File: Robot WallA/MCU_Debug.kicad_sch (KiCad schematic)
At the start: 10 parts, among them J11 USB_B_Micro, U5 FT230XS

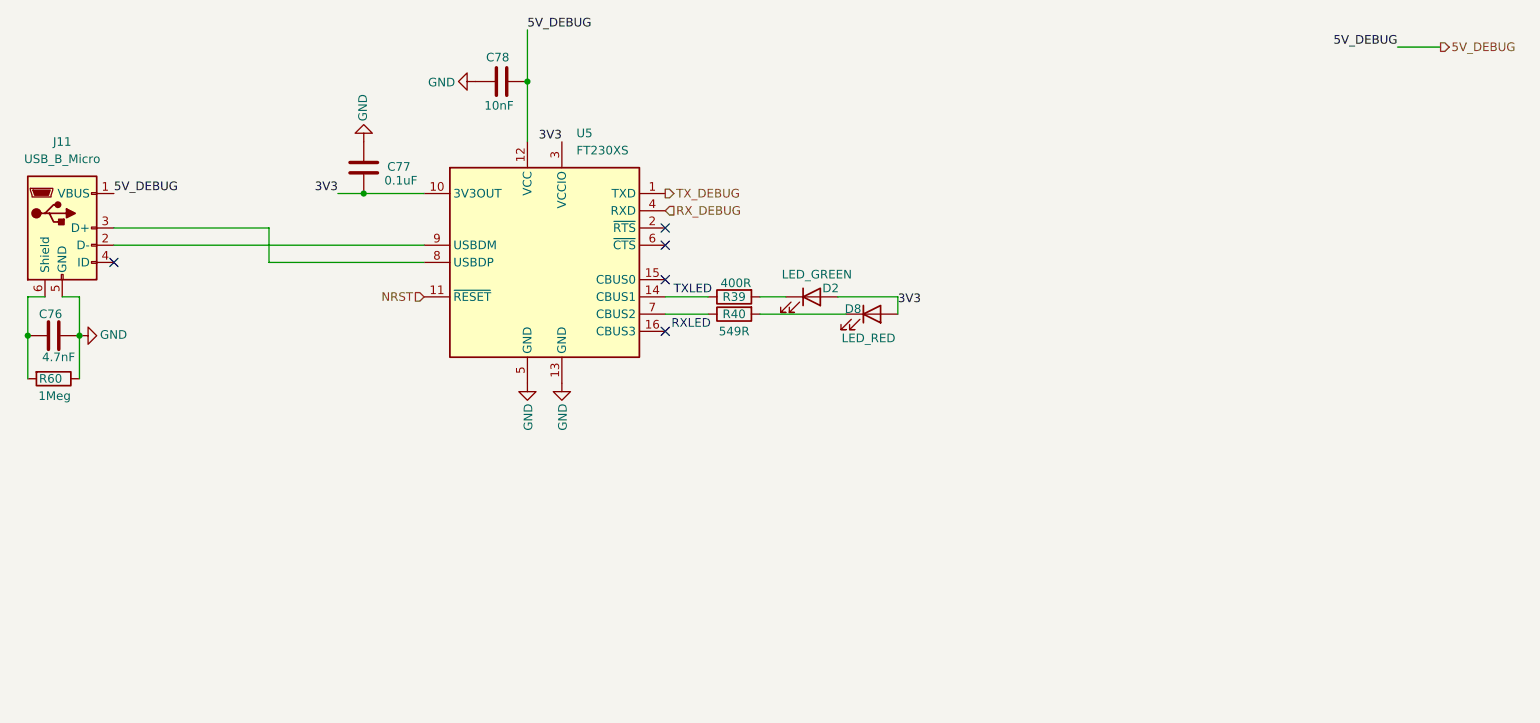
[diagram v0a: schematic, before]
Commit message: Continued to link MCU pins, Added a sheet for servomotors and optional 2 DC motors.
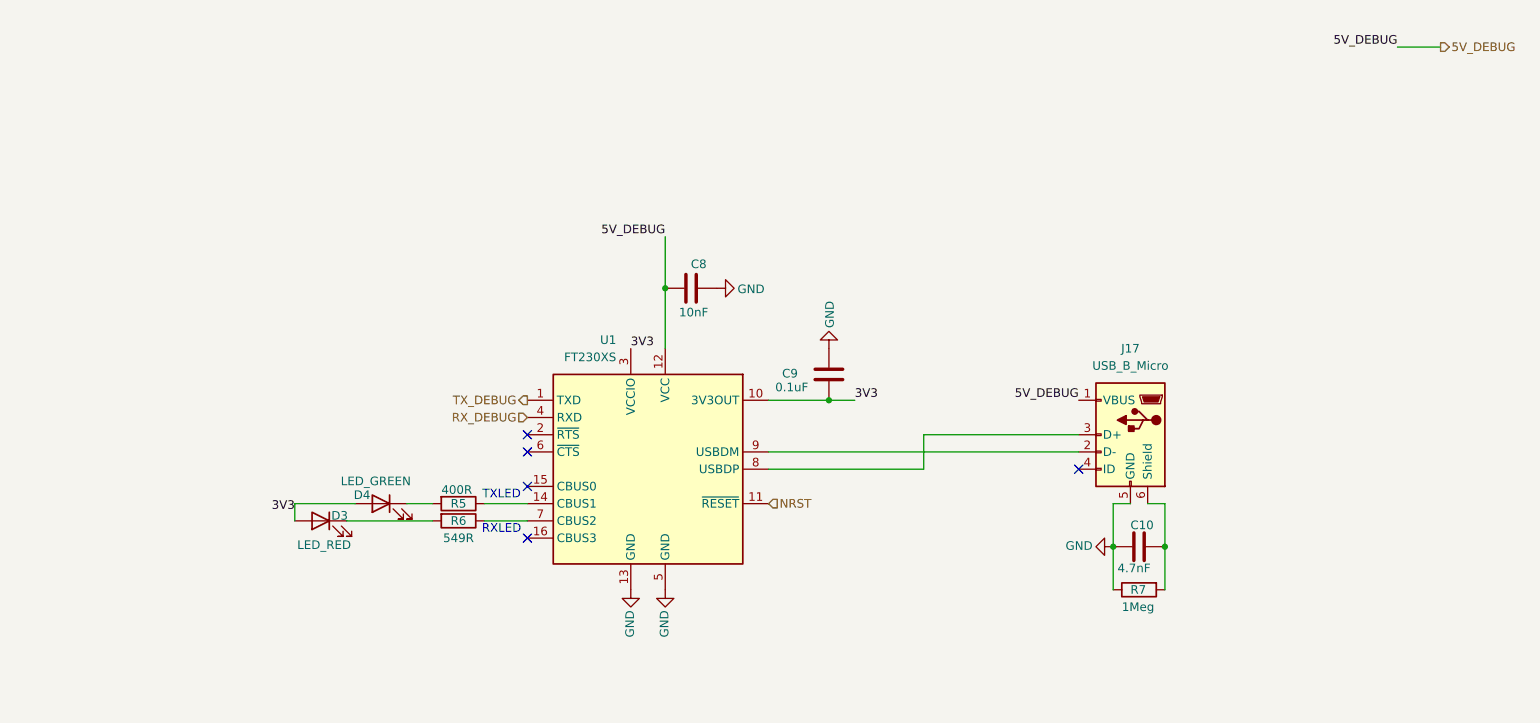
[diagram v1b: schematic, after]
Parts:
- renumbered C76 to C10, C78 to C8, C77 to C9, D8 to D3, D2 to D4, J11 to J17, R39 to R5, R40 to R6, R60 to R7, U5 to U1
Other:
- moved on the sheet: C10, C8, C9, D3, D4, J17, R5, R6, R7, U1

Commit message: Defined every footprints
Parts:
- C34: renamed from C9; value 0.1uF -> 100nF
- R27: renamed from R5; footprint Resistor_SMD:R_0603_1608Metric -> Resistor_SMD:R_0603_1608Metric_Pad0.98x0.95mm_HandSolder
- R28: renamed from R6; footprint Resistor_SMD:R_0603_1608Metric -> Resistor_SMD:R_0603_1608Metric_Pad0.98x0.95mm_HandSolder; Manufacturer_Part_Number RC0603FR-07549RL -> (none)
- renumbered C8 to C33, C10 to C35, D4 to D1, D3 to D2, J17 to J4, R7 to R29
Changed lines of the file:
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@@
 		(on_board yes)
 		(dnp no)
-		(property "Reference" "#PWR023"
+		(property "Reference" "#PWR038"
 			(at 130.81 106.68 0)
 			(effects
@@
 			(project "PCB"
 				(path "/117fd49e-499d-4b54-b58c-f6b538ecca4a/b9176f6a-4299-4bca-a59b-5ff3df09c616/17777bae-0c68-45a7-8f55-4db398213b8b"
-					(reference "#PWR023")
+					(reference "#PWR038")
 					(unit 1)
 				)
@@
 		(on_board yes)
 		(dnp no)
-		(property "Reference" "D3"
+		(property "Reference" "D2"
 			(at 87.884 89.408 0)
 			(effects
@@
 			)
 		)
-		(property "Sim.Pins" "1=K 2=A"
-			(at 85.09 90.17 0)
-			(effects
-				(font
-					(size 1.27 1.27)
-				)
-				(hide yes)
-			)
-		)
 		(pin "2"
 		)
@@
 			(project "PCB"
 				(path "/117fd49e-499d-4b54-b58c-f6b538ecca4a/b9176f6a-4299-4bca-a59b-5ff3df09c616/17777bae-0c68-45a7-8f55-4db398213b8b"
-					(reference "D3")
+					(reference "D2")
 					(unit 1)
 				)
@@
 		(on_board yes)
 		(dnp no)
-		(property "Reference" "#PWR027"
+		(property "Reference" "#PWR037"
 			(at 195.58 93.98 0)
 			(effects
@@
 			(project "PCB"
 				(path "/117fd49e-499d-4b54-b58c-f6b538ecca4a/b9176f6a-4299-4bca-a59b-5ff3df09c616/17777bae-0c68-45a7-8f55-4db398213b8b"
-					(reference "#PWR027")
+					(reference "#PWR037")
 					(unit 1)
 				)
@@
 		(on_board yes)
 		(dnp no)
-		(property "Reference" "R7"
+		(property "Reference" "R29"
 			(at 204.47 100.33 90)
 			(effects
@@
 			(project "PCB"
 				(path "/117fd49e-499d-4b54-b58c-f6b538ecca4a/b9176f6a-4299-4bca-a59b-5ff3df09c616/17777bae-0c68-45a7-8f55-4db398213b8b"
-					(reference "R7")
+					(reference "R29")
 					(unit 1)
 				)
@@
 		(on_board yes)
 		(dnp no)
-		(property "Reference" "C10"
+		(property "Reference" "C35"
 			(at 204.47 90.805 90)
 			(effects
@@
 			(project "PCB"
 				(path "/117fd49e-499d-4b54-b58c-f6b538ecca4a/b9176f6a-4299-4bca-a59b-5ff3df09c616/17777bae-0c68-45a7-8f55-4db398213b8b"
-					(reference "C10")
+					(reference "C35")
 					(unit 1)
 				)
@@
 		(on_board yes)
 		(dnp no)
-		(property "Reference" "#PWR026"
+		(property "Reference" "#PWR036"
 			(at 160.02 58.42 0)
 			(effects
@@
 			(project "PCB"
 				(path "/117fd49e-499d-4b54-b58c-f6b538ecca4a/b9176f6a-4299-4bca-a59b-5ff3df09c616/17777bae-0c68-45a7-8f55-4db398213b8b"
-					(reference "#PWR026")
+					(reference "#PWR036")
 					(unit 1)
 				)
@@
 		(on_board yes)
 		(dnp no)
-		(property "Reference" "#PWR025"
+		(property "Reference" "#PWR035"
 			(at 149.86 55.88 0)
 			(effects
@@
 			(project "PCB"
 				(path "/117fd49e-499d-4b54-b58c-f6b538ecca4a/b9176f6a-4299-4bca-a59b-5ff3df09c616/17777bae-0c68-45a7-8f55-4db398213b8b"
-					(reference "#PWR025")
+					(reference "#PWR035")
 					(unit 1)
 				)
@@
 		(on_board yes)
 		(dnp no)
-		(property "Reference" "D4"
+		(property "Reference" "D1"
 			(at 91.186 86.36 0)
 			(effects
@@
 			(project "PCB"
 				(path "/117fd49e-499d-4b54-b58c-f6b538ecca4a/b9176f6a-4299-4bca-a59b-5ff3df09c616/17777bae-0c68-45a7-8f55-4db398213b8b"
-					(reference "D4")
+					(reference "D1")
 					(unit 1)
 				)
@@
 		(dnp no)
 		(fields_autoplaced yes)
-		(property "Reference" "J17"
+		(property "Reference" "J4"
 			(at 204.47 64.77 0)
 			(effects
@@
 			(project ""
 				(path "/117fd49e-499d-4b54-b58c-f6b538ecca4a/b9176f6a-4299-4bca-a59b-5ff3df09c616/17777bae-0c68-45a7-8f55-4db398213b8b"
-					(reference "J17")
+					(reference "J4")
 					(unit 1)
 				)
@@
 		(on_board yes)
 		(dnp no)
-		(property "Reference" "R6"
+		(property "Reference" "R28"
 			(at 105.41 90.17 90)
 			(effects
@@
 			)
 		)
-		(property "Footprint" "Resistor_SMD:R_0603_1608Metric"
+		(property "Footprint" "Resistor_SMD:R_0603_1608Metric_Pad0.98x0.95mm_HandSolder"
 			(at 105.41 88.392 90)
 			(effects
@@
 			)
 		)
-		(property "Manufacturer_Part_Number" "RC0603FR-07549RL "
+		(property "Manufacturer_Part_Number" ""
 			(at 105.41 90.17 0)
 			(effects
@@
 			(project "PCB"
 				(path "/117fd49e-499d-4b54-b58c-f6b538ecca4a/b9176f6a-4299-4bca-a59b-5ff3df09c616/17777bae-0c68-45a7-8f55-4db398213b8b"
-					(reference "R6")
+					(reference "R28")
 					(unit 1)
 				)
@@
 		(on_board yes)
 		(dnp no)
-		(property "Reference" "C9"
+		(property "Reference" "C34"
 			(at 153.1198 68.4452 0)
 			(effects
@@
 			)
 		)
-		(property "Value" "0.1uF"
+		(property "Value" "100nF"
 			(at 152.1038 70.4772 0)
 			(effects
@@
 			(project "PCB"
 				(path "/117fd49e-499d-4b54-b58c-f6b538ecca4a/b9176f6a-4299-4bca-a59b-5ff3df09c616/17777bae-0c68-45a7-8f55-4db398213b8b"
-					(reference "C9")
+					(reference "C34")
 					(unit 1)
 				)
@@
 		(on_board yes)
 		(dnp no)
-		(property "Reference" "R5"
+		(property "Reference" "R27"
 			(at 105.41 87.63 90)
 			(effects
@@
 			)
 		)
-		(property "Footprint" "Resistor_SMD:R_0603_1608Metric"
+		(property "Footprint" "Resistor_SMD:R_0603_1608Metric_Pad0.98x0.95mm_HandSolder"
 			(at 105.41 85.852 90)
 			(effects
@@
 			(project "PCB"
 				(path "/117fd49e-499d-4b54-b58c-f6b538ecca4a/b9176f6a-4299-4bca-a59b-5ff3df09c616/17777bae-0c68-45a7-8f55-4db398213b8b"
-					(reference "R5")
+					(reference "R27")
 					(unit 1)
 				)
@@
 		(on_board yes)
 		(dnp no)
-		(property "Reference" "#PWR024"
+		(property "Reference" "#PWR039"
 			(at 135.89 106.68 0)
 			(effects
@@
 			(project "PCB"
 				(path "/117fd49e-499d-4b54-b58c-f6b538ecca4a/b9176f6a-4299-4bca-a59b-5ff3df09c616/17777bae-0c68-45a7-8f55-4db398213b8b"
-					(reference "#PWR024")
+					(reference "#PWR039")
 					(unit 1)
 				)
@@
 		(on_board yes)
 		(dnp no)
-		(property "Reference" "C8"
+		(property "Reference" "C33"
 			(at 141.986 52.324 90)
 			(effects
@@
 			(project "PCB"
 				(path "/117fd49e-499d-4b54-b58c-f6b538ecca4a/b9176f6a-4299-4bca-a59b-5ff3df09c616/17777bae-0c68-45a7-8f55-4db398213b8b"
-					(reference "C8")
-					(unit 1)
-				)
+					(reference "C33")
+					(unit 1)
+				)

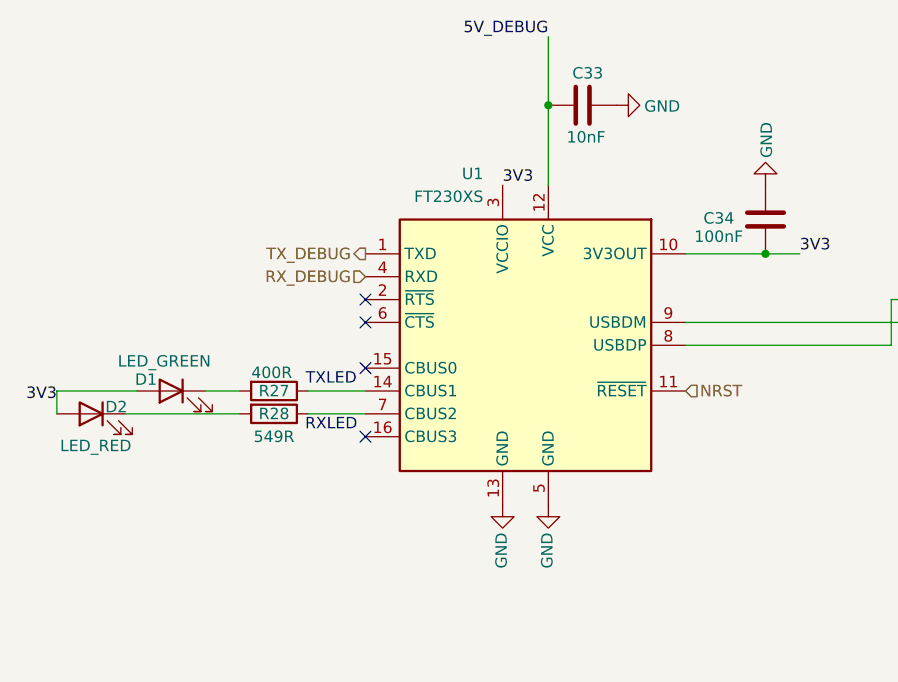
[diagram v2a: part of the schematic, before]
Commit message: Updated USB UART converter, Linked telemeter sensors.
Updated components indicators
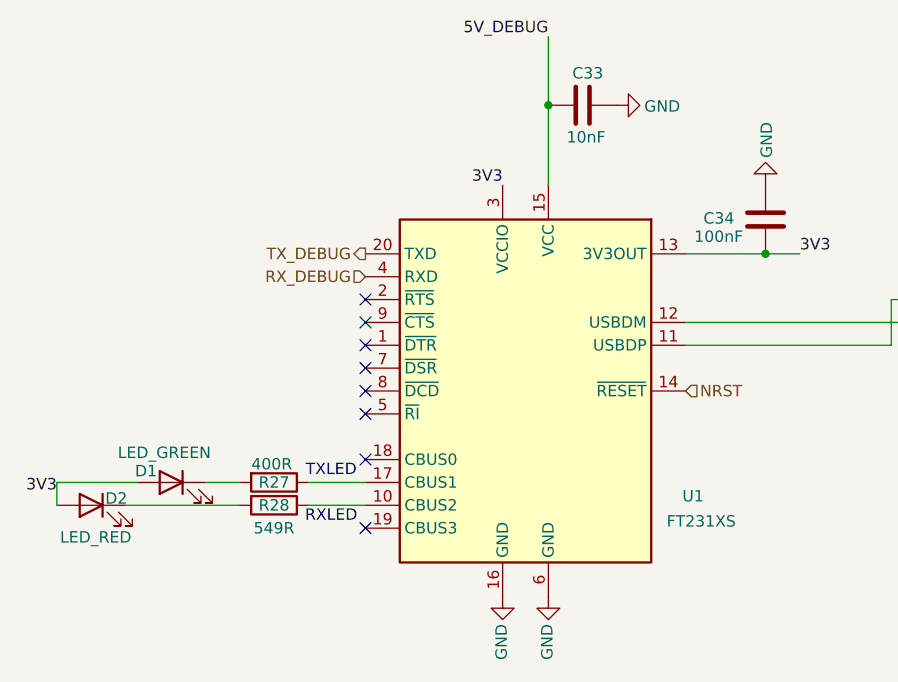
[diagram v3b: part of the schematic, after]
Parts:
- removed U1: FT230XS, Package_SO:SSOP-16_3.9x4.9mm_P0.635mm, symbol Interface_USB:FT230XS
- added U1: FT231XS, Package_SO:SSOP-20_3.9x8.7mm_P0.635mm, symbol Interface_USB:FT231XS
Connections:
- net 3V3: now also U1.13 (3V3OUT), U1.3 (VCCIO)
- net 5V_DEBUG: now also U1.15 (VCC)
- net GND: now also U1.16 (GND), U1.6 (GND)
- net NRST: now also U1.14 (~{RESET})
- net RX_DEBUG: now also U1.4 (RXD)
- net TX_DEBUG: now also U1.20 (TXD)
- net at J4.2 (D-): now also U1.12 (USBDM)
- net at J4.3 (D+): now also U1.11 (USBDP)
- net at R28.1: now also U1.10 (CBUS2)
- net at R27.1: now also U1.17 (CBUS1)
- no-connect marks 5 -> 9

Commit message: Continue to route
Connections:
- net D-: now reaches J4.2 (D-), U1.12 (USBDM)
- net D+: now reaches J4.3 (D+), U1.11 (USBDP)
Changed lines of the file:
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@@
+		)
+	)
+	(label "D-"
+		(at 158.75 80.01 0)
+		(effects
+			(font
+				(size 1.27 1.27)
+				(thickness 0.254)
+				(bold yes)
+			)
+			(justify left bottom)
+		)
+	)
+	(label "D+"
+		(at 158.75 82.55 0)
+		(effects
+			(font
+				(size 1.27 1.27)
+				(thickness 0.254)
+				(bold yes)
+			)
+			(justify left bottom)
+		)
+	)
+	(label "D+"
+		(at 196.85 114.3 180)
+		(effects
+			(font
+				(size 1.27 1.27)
+				(thickness 0.254)
+				(bold yes)
+			)
+			(justify right bottom)
+		)
+	)
+	(label "D-"
+		(at 196.85 116.84 180)
+		(effects
+			(font
+				(size 1.27 1.27)
+				(thickness 0.254)
+				(bold yes)
+			)
+			(justify right bottom)
 		)
 	)
@@
 		)
 	)
+	(netclass_flag ""
+		(length 2.54)
+		(shape round)
+		(at 196.85 114.3 270)
+		(effects
+			(font
+				(size 1.27 1.27)
+			)
+			(justify right bottom)
+		)
+		(property "Netclass" "DiffPair_90R"
+			(at 201.168 114.3 0)
+			(effects
+				(font
+					(size 1.27 1.27)
+				)
+				(justify left)
+			)
+		)
+		(property "Component Class" ""
+			(at -116.84 -41.91 0)
+			(effects
+				(font
+					(size 1.27 1.27)
+					(italic yes)
+				)
+			)
+		)
+	)
+	(netclass_flag ""
+		(length 2.54)
+		(shape round)
+		(at 196.85 116.84 270)
+		(effects
+			(font
+				(size 1.27 1.27)
+			)
+			(justify right bottom)
+		)
+		(property "Netclass" "DiffPair_90R"
+			(at 201.168 116.84 0)
+			(effects
+				(font
+					(size 1.27 1.27)
+				)
+				(justify left)
+			)
+		)
+		(property "Component Class" ""
+			(at -116.84 -39.37 0)
+			(effects
+				(font
+					(size 1.27 1.27)
+					(italic yes)
+				)
+			)
+		)
+	)

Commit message: Updated fab files.
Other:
- company: (none) -> Socotec Monitoring
- title: (none) -> Robot Wall-A
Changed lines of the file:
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@@
 	(generator_version "9.0")
 	(paper "A4")
+	(title_block
+		(title "Robot Wall-A")
+		(date "2025-09-20")
+		(rev "v1.0")
+		(company "Socotec Monitoring")
+		(comment 1 "GDU")
+		(comment 2 "THO")
+	)
 	(text "TXLED"
 		(exclude_from_sim no)
@@
 			)
 		)
+		(property "MPN" ""
+			(at 85.09 100.33 0)
+			(effects
+				(font
+					(size 1.27 1.27)
+				)
+				(hide yes)
+			)
+		)
 		(pin "2"
 		)
@@
 			)
 		)
+		(property "MPN" ""
+			(at 205.74 100.33 90)
+			(effects
+				(font
+					(size 1.27 1.27)
+				)
+				(hide yes)
+			)
+		)
 		(pin "1"
 		)
@@
 			)
 		)
+		(property "MPN" ""
+			(at 205.74 93.98 90)
+			(effects
+				(font
+					(size 1.27 1.27)
+				)
+				(hide yes)
+			)
+		)
 		(pin "1"
 		)
@@
 		(property "Manufacturer_Part_Number" ""
 			(at 105.41 100.33 0)
+			(effects
+				(font
+					(size 1.27 1.27)
+				)
+				(hide yes)
+			)
+		)
+		(property "MPN" ""
+			(at 105.41 100.33 90)
 			(effects
 				(font
@@
 			)
 		)
+		(property "MPN" ""
+			(at 204.47 77.47 0)
+			(effects
+				(font
+					(size 1.27 1.27)
+				)
+				(hide yes)
+			)
+		)
 		(pin "4"
 		)
@@
 			)
 		)
+		(property "MPN" ""
+			(at 160.02 68.58 0)
+			(effects
+				(font
+					(size 1.27 1.27)
+				)
+				(hide yes)
+			)
+		)
 		(pin "1"
 		)
@@
 			)
 		)
+		(property "MPN" ""
+			(at 133.35 87.63 0)
+			(effects
+				(font
+					(size 1.27 1.27)
+				)
+				(hide yes)
+			)
+		)
 		(pin "6"
 		)
@@
 			)
 		)
+		(property "MPN" ""
+			(at 93.98 97.79 0)
+			(effects
+				(font
+					(size 1.27 1.27)
+				)
+				(hide yes)
+			)
+		)
 		(pin "2"
 		)
@@
 			)
 		)
+		(property "MPN" ""
+			(at 139.7 55.88 90)
+			(effects
+				(font
+					(size 1.27 1.27)
+				)
+				(hide yes)
+			)
+		)
 		(pin "1"
 		)
@@
 			(effects
 				(font
+					(size 1.27 1.27)
+				)
+				(hide yes)
+			)
+		)
+		(property "MPN" ""
+			(at 105.41 97.79 90)
+			(effects
+				(font

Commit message: Modified footprint to simplify BOM. Finalized BOM.
Updated fab files
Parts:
- C33: value 10nF -> 10nF/50V; footprint Capacitor_SMD:C_0603_1608Metric_Pad1.08x0.95mm_HandSolder -> Capacitor_SMD:C_0805_2012Metric_Pad1.18x1.45mm_HandSolder; Manufacturer_Part_Number (none) -> CL21B103KBANNNC
- C34: Manufacturer_Part_Number (none) -> KGM15BR71H104KT
- C35: Manufacturer_Part_Number (none) -> CC0603JRX7R8BB472
- R27: value 400R -> 402R; Manufacturer_Part_Number (none) -> CR0603-FX-4020ELF
- R28: Manufacturer_Part_Number (none) -> RC0603FR-07549RL
- R29: Manufacturer_Part_Number (none) -> ERJ-3GEYJ105V
